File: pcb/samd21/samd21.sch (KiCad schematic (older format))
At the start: 5 parts

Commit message: got most of the parts down..
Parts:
- added C1: 1uF, Capacitor_SMD:C_0805_2012Metric, symbol Device:C_Small
- added D1: red LED, LED_SMD:LED_0805_2012Metric, symbol Device:LED_Small
- added MX1, MX2, MX3: MX-NoLED, MX_Alps_Hybrid:MX-1U-NoLED, symbol MX_Alps_Hybrid:MX-NoLED
- added R1: 1.5K, Resistor_SMD:R_0805_2012Metric, symbol Device:R_Small
- added SW1: SW_Push, random_parts2:SKQG-1155865, symbol Switch:SW_Push
- C2, C3: renamed from C?; footprint (none) -> Capacitor_SMD:C_0805_2012Metric
- USB1: renamed from USB?; footprint (none) -> random_parts2:Molex-0548190589
- gave numbers to parts that had none: 2
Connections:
- net 3v is gone; now on net +3V3: C3.1, U1.5 (OUT)
- net GND: now also U2.10 (GND), U2.28 (GND), C1.1, D1.1 (K), SW1.1
- net KEY3: now reaches U2.11 (PA08)
- net KEY3: now also MX3.2 (ROW)
- net at U2.13 (PA10): now also R1.1
- net D-: now reaches U2.23 (PA24)
- net D-: now also USB1.4 (D-)
- net D+: now reaches U2.24 (PA25)
- net D+: now also USB1.3 (D+)
- net at U2.26 (~RESET): now also SW1.2
- net at U2.29 (VDDCORE): now also C1.2
- net +3V3: now reaches U2.30 (VDDIN)
- net +3V3: now also U2.9 (VDDANA), MX1.1 (COL), MX2.1 (COL), MX3.1 (COL)
- net SWCLK: now reaches U2.31 (PA30)
- net SWDIO: now reaches U2.32 (PA31)
- net KEY1: now reaches U2.7 (PA06)
- net KEY1: now also MX1.2 (ROW)
- net KEY2: now reaches U2.8 (PA07)
- net KEY2: now also MX2.2 (ROW)
- new net: D1.2 (A), R1.2
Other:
- moved on the sheet: C2

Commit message: v1-dev pcb+schem complete. not finished
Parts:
- added J1: Conn_01x04_Male, Connector_PinSocket_2.54mm:PinSocket_1x04_P2.54mm_Vertical, symbol Connector:Conn_01x04_Male
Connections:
- net +3V3: now also J1.1 (Pin_1)
- net GND: now also USB1.6 (SHIELD), J1.4 (Pin_4)
- net KEY1: now also U2.8 (PA07); no longer U2.7 (PA06)
- net KEY2: now also U2.7 (PA06); no longer U2.8 (PA07)
- net KEY3: now also U2.6 (PA05); no longer U2.11 (PA08)
- net SWCLK: now also J1.2 (Pin_2)
- net SWDIO: now also J1.3 (Pin_3)
- net at U2.13 (PA10): no longer R1.1
- net at U2.25 (PA27): now also R1.1
- net 5V: now reaches C2.1, U1.1 (IN), U1.3 (EN), USB1.5 (VBUS)
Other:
- moved on the sheet: D1, R1
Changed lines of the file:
@@
 L Device:R_Small R1
 U 1 1 611A96BE
-P 3900 3900
-F 0 "R1" V 3704 3900 50  0000 C CNN
-F 1 "1.5K" V 3795 3900 50  0000 C CNN
-F 2 "Resistor_SMD:R_0805_2012Metric" H 3900 3900 50  0001 C CNN
-F 3 "~" H 3900 3900 50  0001 C CNN
-	1    3900 3900
+P 3850 5600
+F 0 "R1" V 3654 5600 50  0000 C CNN
+F 1 "1.5K" V 3745 5600 50  0000 C CNN
+F 2 "Resistor_SMD:R_0805_2012Metric" H 3850 5600 50  0001 C CNN
+F 3 "~" H 3850 5600 50  0001 C CNN
+	1    3850 5600
 	0    1    1    0
 $EndComp
@@
 L Device:LED_Small D1
 U 1 1 611ADBE8
-P 3650 4100
-F 0 "D1" V 3696 4030 50  0000 R CNN
-F 1 "red LED" V 3605 4030 50  0000 R CNN
-F 2 "LED_SMD:LED_0805_2012Metric" V 3650 4100 50  0001 C CNN
-F 3 "~" V 3650 4100 50  0001 C CNN
-	1    3650 4100
+P 3600 5800
+F 0 "D1" V 3646 5730 50  0000 R CNN
+F 1 "red LED" V 3555 5730 50  0000 R CNN
+F 2 "LED_SMD:LED_0805_2012Metric" V 3600 5800 50  0001 C CNN
+F 3 "~" V 3600 5800 50  0001 C CNN
+	1    3600 5800
 	0    -1   -1   0
 $EndComp
@@
 L power:GND #PWR0107
 U 1 1 611B1405
-P 3650 4350
-F 0 "#PWR0107" H 3650 4100 50  0001 C CNN
-F 1 "GND" H 3655 4177 50  0000 C CNN
-F 2 "" H 3650 4350 50  0001 C CNN
-F 3 "" H 3650 4350 50  0001 C CNN
-	1    3650 4350
-	1    0    0    -1
-$EndComp
-Wire Wire Line
-	4200 3900 4000 3900
-Wire Wire Line
-	3800 3900 3650 3900
-Wire Wire Line
-	3650 3900 3650 4000
-Wire Wire Line
-	3650 4200 3650 4350
-Text GLabel 4200 3700 0    50   Input ~ 0
+P 3600 6050
+F 0 "#PWR0107" H 3600 5800 50  0001 C CNN
+F 1 "GND" H 3605 5877 50  0000 C CNN
+F 2 "" H 3600 6050 50  0001 C CNN
+F 3 "" H 3600 6050 50  0001 C CNN
+	1    3600 6050
+	1    0    0    -1
+$EndComp
+Wire Wire Line
+	3750 5600 3600 5600
+Wire Wire Line
+	3600 5600 3600 5700
+Wire Wire Line
+	3600 5900 3600 6050
+Text GLabel 4200 3400 0    50   Input ~ 0
 KEY3
+Text GLabel 4200 3500 0    50   Input ~ 0
+KEY2
 Text GLabel 4200 3600 0    50   Input ~ 0
-KEY2
-Text GLabel 4200 3500 0    50   Input ~ 0
 KEY1
 $Comp
@@
 	1    0    0    -1
 $EndComp
+$Comp
+L Connector:Conn_01x04_Male J1
+U 1 1 61174EBA
+P 2900 5650
+F 0 "J1" H 3008 5931 50  0000 C CNN
+F 1 "Conn_01x04_Male" H 3008 5840 50  0000 C CNN
+F 2 "Connector_PinSocket_2.54mm:PinSocket_1x04_P2.54mm_Vertical" H 2900 5650 50  0001 C CNN
+F 3 "~" H 2900 5650 50  0001 C CNN
+	1    2900 5650
+	1    0    0    -1
+$EndComp
+$Comp
+L power:+3V3 #PWR0111
+U 1 1 611766B7
+P 3400 5400
+F 0 "#PWR0111" H 3400 5250 50  0001 C CNN
+F 1 "+3V3" H 3415 5573 50  0000 C CNN
+F 2 "" H 3400 5400 50  0001 C CNN
+F 3 "" H 3400 5400 50  0001 C CNN
+	1    3400 5400
+	1    0    0    -1
+$EndComp
+Wire Wire Line
+	3400 5400 3400 5550
+Wire Wire Line
+	3400 5550 3100 5550
+Text GLabel 3100 5650 2    50   Input ~ 0
+SWCLK
+Text GLabel 3100 5750 2    50   Input ~ 0
+SWDIO
+$Comp
+L power:GND #PWR0112
+U 1 1 6117911B
+P 3400 6000
+F 0 "#PWR0112" H 3400 5750 50  0001 C CNN
+F 1 "GND" H 3405 5827 50  0000 C CNN
+F 2 "" H 3400 6000 50  0001 C CNN
+F 3 "" H 3400 6000 50  0001 C CNN
+	1    3400 6000
+	1    0    0    -1
+$EndComp
+Wire Wire Line
+	3100 5850 3400 5850
+Wire Wire Line
+	3400 5850 3400 6000
+Text Label 1750 3000 0    50   ~ 0
+5V
+Wire Wire Line
+	3950 5600 4200 5600
+Wire Wire Line
+	1600 2900 1600 2800
+Wire Wire Line
+	1600 2800 1000 2800
+Wire Wire Line
+	1000 2800 1000 3500
+Wire Wire Line
+	1000 3500 1600 3500
+Wire Wire Line
+	1600 3500 1600 3400
+Connection ~ 1600 3400
 $EndSCHEMATC

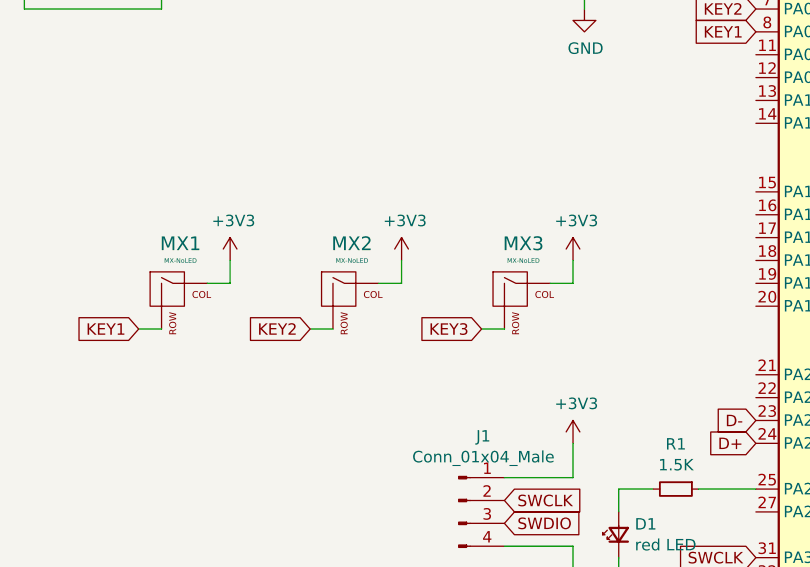
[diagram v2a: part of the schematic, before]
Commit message: moved switches from 3v3 to GND, using pullup
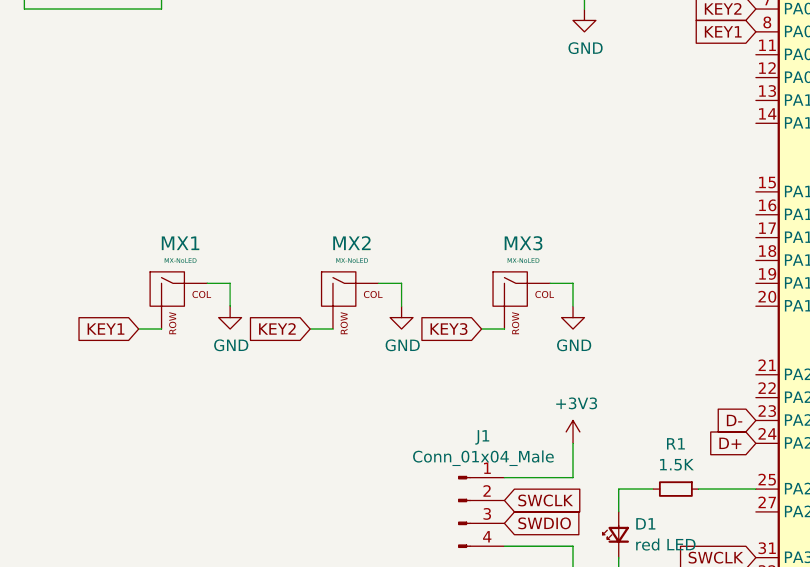
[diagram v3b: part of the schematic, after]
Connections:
- net +3V3: no longer MX1.1 (COL), MX2.1 (COL), MX3.1 (COL)
- net GND: now also MX1.1 (COL), MX2.1 (COL), MX3.1 (COL)
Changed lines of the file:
@@
 Text GLabel 1500 4900 0    50   Input ~ 0
 KEY1
-$Comp
-L power:+3V3 #PWR0108
-U 1 1 611BEDF3
-P 1900 4600
-F 0 "#PWR0108" H 1900 4450 50  0001 C CNN
-F 1 "+3V3" H 1915 4773 50  0000 C CNN
-F 2 "" H 1900 4600 50  0001 C CNN
-F 3 "" H 1900 4600 50  0001 C CNN
-	1    1900 4600
-	1    0    0    -1
-$EndComp
-Wire Wire Line
-	1900 4600 1900 4700
 Wire Wire Line
 	1900 4700 1800 4700
@@
 Text GLabel 2250 4900 0    50   Input ~ 0
 KEY2
-$Comp
-L power:+3V3 #PWR0109
-U 1 1 611CAF3A
-P 2650 4600
-F 0 "#PWR0109" H 2650 4450 50  0001 C CNN
-F 1 "+3V3" H 2665 4773 50  0000 C CNN
-F 2 "" H 2650 4600 50  0001 C CNN
-F 3 "" H 2650 4600 50  0001 C CNN
-	1    2650 4600
-	1    0    0    -1
-$EndComp
-Wire Wire Line
-	2650 4600 2650 4700
 Wire Wire Line
 	2650 4700 2550 4700
@@
 Text GLabel 3000 4900 0    50   Input ~ 0
 KEY3
-$Comp
-L power:+3V3 #PWR0110
-U 1 1 611CD00C
-P 3400 4600
-F 0 "#PWR0110" H 3400 4450 50  0001 C CNN
-F 1 "+3V3" H 3415 4773 50  0000 C CNN
-F 2 "" H 3400 4600 50  0001 C CNN
-F 3 "" H 3400 4600 50  0001 C CNN
-	1    3400 4600
-	1    0    0    -1
-$EndComp
-Wire Wire Line
-	3400 4600 3400 4700
 Wire Wire Line
 	3400 4700 3300 4700
@@
 	1600 3500 1600 3400
 Connection ~ 1600 3400
+$Comp
+L power:GND #PWR?
+U 1 1 61181268
+P 1900 4800
+F 0 "#PWR?" H 1900 4550 50  0001 C CNN
+F 1 "GND" H 1905 4627 50  0000 C CNN
+F 2 "" H 1900 4800 50  0001 C CNN
+F 3 "" H 1900 4800 50  0001 C CNN
+	1    1900 4800
+	1    0    0    -1
+$EndComp
+Wire Wire Line
+	1900 4700 1900 4800
+$Comp
+L power:GND #PWR?
+U 1 1 61183AE4
+P 2650 4800
+F 0 "#PWR?" H 2650 4550 50  0001 C CNN
+F 1 "GND" H 2655 4627 50  0000 C CNN
+F 2 "" H 2650 4800 50  0001 C CNN
+F 3 "" H 2650 4800 50  0001 C CNN
+	1    2650 4800
+	1    0    0    -1
+$EndComp
+Wire Wire Line
+	2650 4700 2650 4800
+$Comp
+L power:GND #PWR?
+U 1 1 61184EC6
+P 3400 4800
+F 0 "#PWR?" H 3400 4550 50  0001 C CNN
+F 1 "GND" H 3405 4627 50  0000 C CNN
+F 2 "" H 3400 4800 50  0001 C CNN
+F 3 "" H 3400 4800 50  0001 C CNN
+	1    3400 4800
+	1    0    0    -1
+$EndComp
+Wire Wire Line
+	3400 4700 3400 4800
 $EndSCHEMATC
